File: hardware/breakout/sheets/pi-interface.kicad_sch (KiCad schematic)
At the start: 27 parts, among them J10 Barcode spare 1, J11 Barcode spare 2, J12 Barcode spare 3, J13 Eye camera trigger out (BNC), J14 Behavior camera trigger out 1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, J15 Behavior camera trigger out 2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, J16 Behavior camera trigger out 3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, J17 Behavior camera trigger out 4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, J18 Internal USB-A (sync-module p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, J7 Sync-module 40-pin GPIO heade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, J8 Barcode -> NI optocoupler (Ta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, J9 Barcode -> Intan optocoupler 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, U14 SN74LVC541APW, U15 SN74AHCT541PW, U74 SN74AHCT541PW

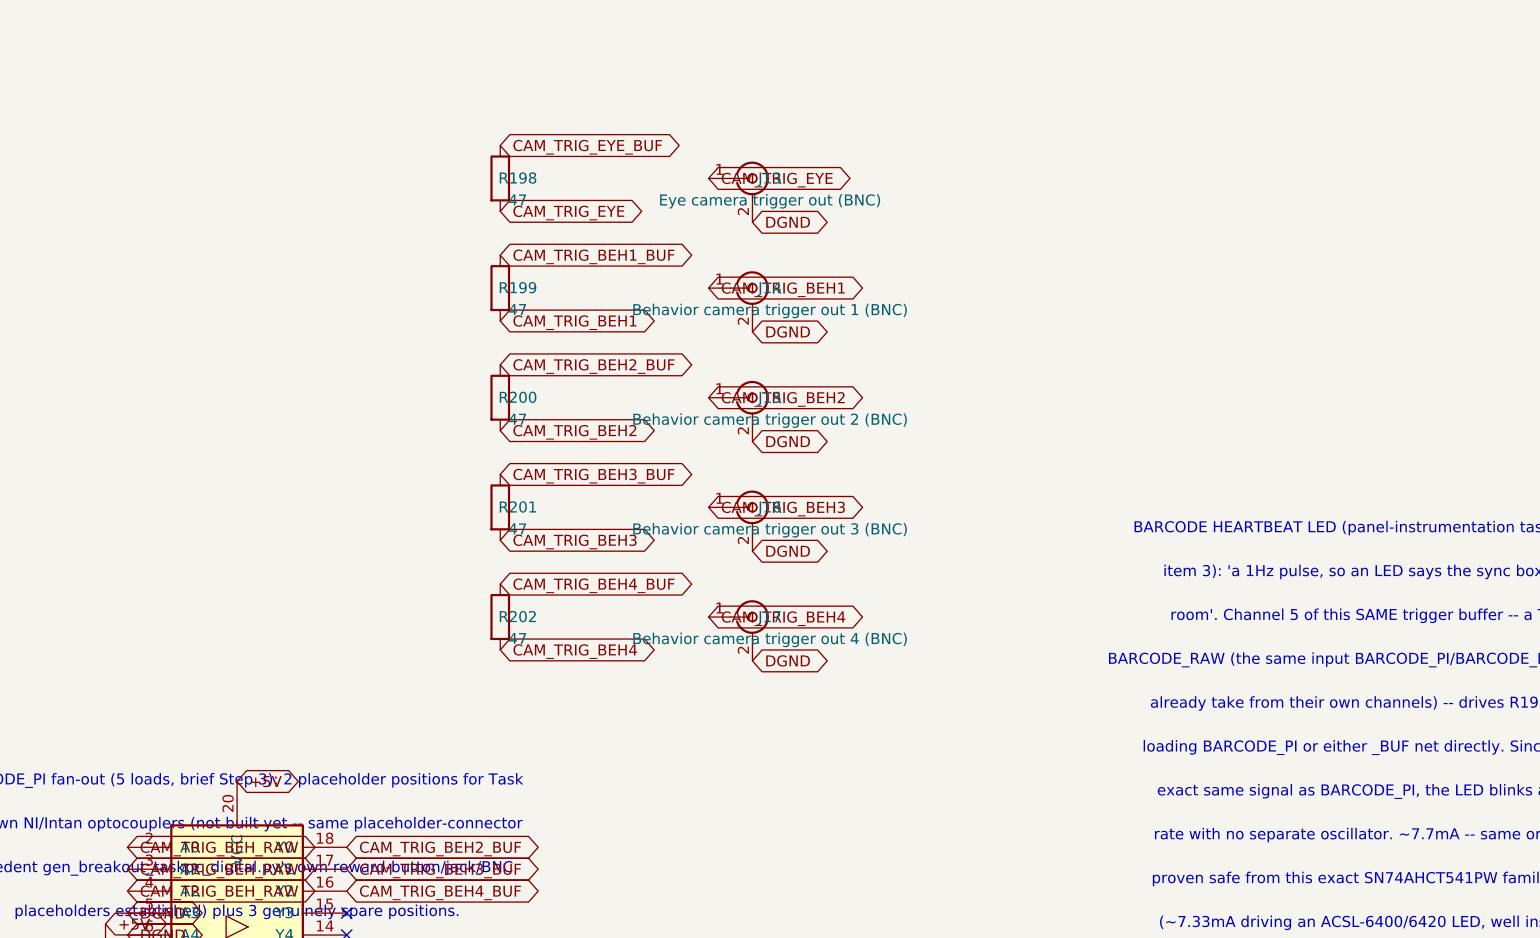
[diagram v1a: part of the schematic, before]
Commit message: fix(hardware): rebuild the connectors on their primary drawings (F6, R1, D3)
Audit step 5, the mechanical half. Three connectors changed, one of them a
fab-stopper, and none of it was visible to the netlist.

MDR68 (the fab-stopper). Rebuilt from MH drawing 3700-0121-01 rev 3.0. The
as-built footprint drilled contacts at 0.5 mm against a required 0.85 mm -- the
pins do not fit, so the board could not have been assembled -- and laid them out
as 2 rows at 2.84 mm where the drawing shows 4 staggered rows of 17 at 1.905 mm.
The 4-row stagger is what makes an 0.85 mm drill manufacturable at a 1.27 mm
mating pitch at all; the array now spans the drawing's own 41.91 mm exactly,
which is the arithmetic that confirms the reading. The claim made during the
audit that it had "no mounting holes at all" was wrong: it had two, Ø2.79 on
57.9 mm centres against the drawing's Ø2.77 on 57.93.

M12 (ruling R1). M12A_5_Panel is deleted, symbol and footprint and generator
function alike. Its contact geometry was sourced well -- IEC 61076-2-101
A-coding, cross-checked three ways -- and it made no difference, because the part
the design procures (Phoenix 1551833) terminates in AWG 22-20 wire and mounts
through the panel. It has no PCB tails, so no board-mount footprint of any
dimensions could have been right, and as built every cable insertion and every
3-4 N.m tightening loaded PCB pads directly. J1 is now a stock 5-way header where
those flying leads land; the connector stays in the order BOM as chassis
furniture.

BNC (F6). BNC_PanelMountable_Vertical puts the connector axis perpendicular to
the PCB -- a 9.65 mm barrel hole through the board -- so on a 430x240 mm board
lying flat in a 2U chassis all 31 barrels pointed at the lid rather than at the
panels. It also cost 5,654 mm2 of pad and 2,267 mm2 of removed copper on every
layer. Replaced by a right-angle dual jack built from Amphenol drawing 31-6575
rev A: 31 ports on 17 bodies, 3 spare ports, every shell still routed
individually.
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
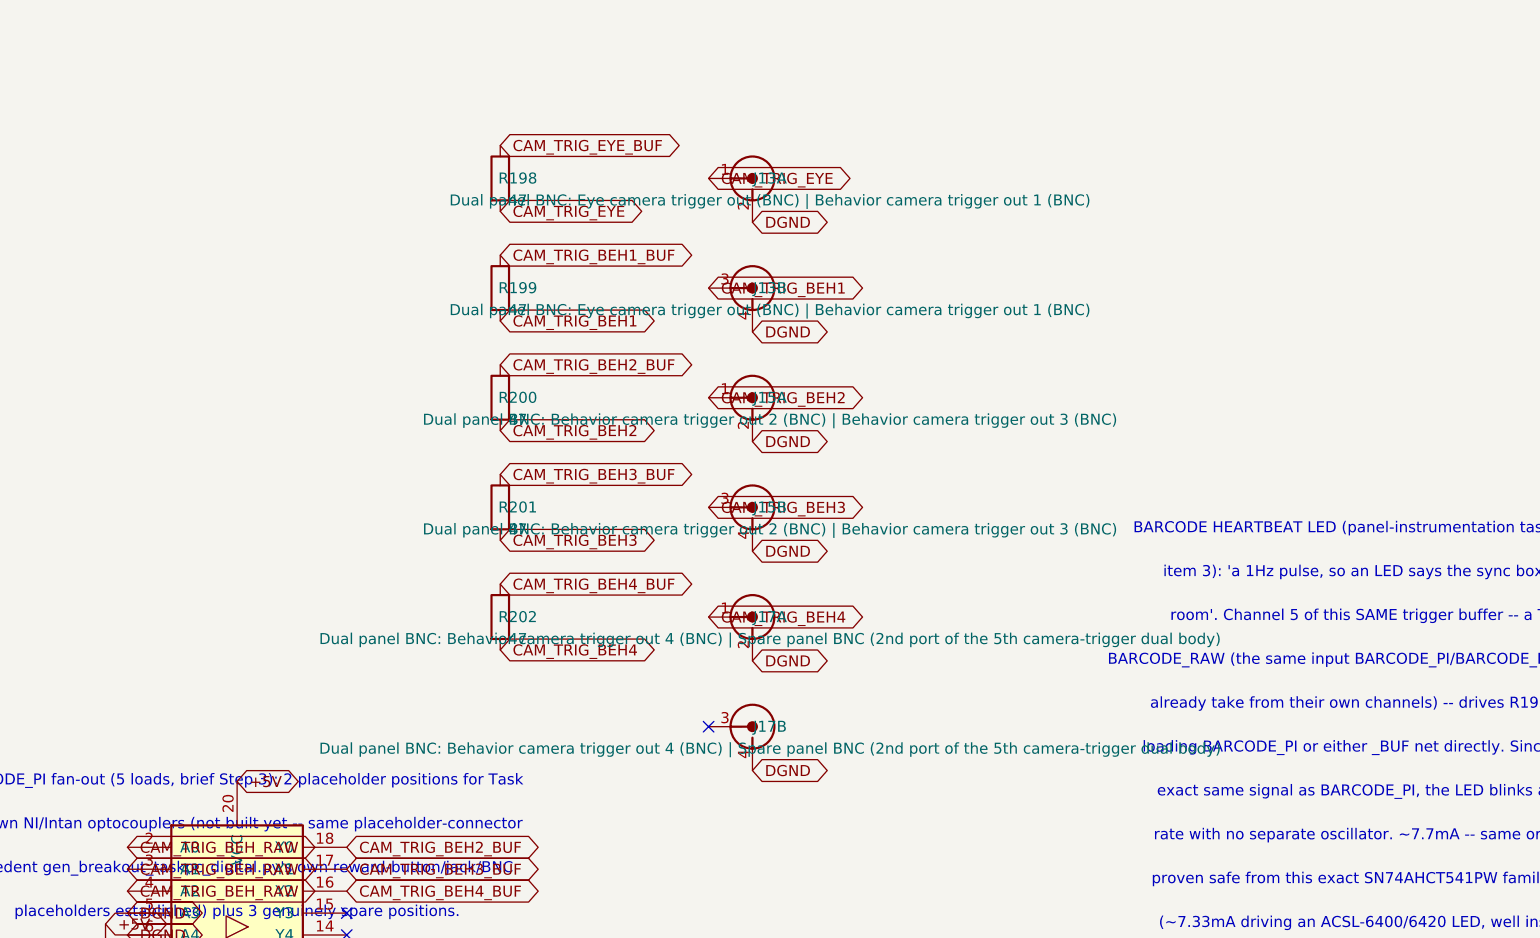
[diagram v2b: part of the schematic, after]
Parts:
- removed J13: Eye camera trigger out (BNC), Connector_Coaxial:BNC_PanelMountable_Vertical, symbol Connector:Conn_Coaxial
- removed J14: Behavior camera trigger out 1 (BNC), Connector_Coaxial:BNC_PanelMountable_Vertical, symbol Connector:Conn_Coaxial
- removed J15: Behavior camera trigger out 2 (BNC), Connector_Coaxial:BNC_PanelMountable_Vertical, symbol Connector:Conn_Coaxial
- removed J16: Behavior camera trigger out 3 (BNC), Connector_Coaxial:BNC_PanelMountable_Vertical, symbol Connector:Conn_Coaxial
- removed J17: Behavior camera trigger out 4 (BNC), Connector_Coaxial:BNC_PanelMountable_Vertical, symbol Connector:Conn_Coaxial
- added J13: Dual panel BNC: Eye camera trigger out (BNC) | Be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, wl-sync:BNC_Dual_RA_Isolated, symbol wl-sync:BNC_Dual_RA_Isolated
- added J15: Dual panel BNC: Behavior camera trigger out 2 (BN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, wl-sync:BNC_Dual_RA_Isolated, symbol wl-sync:BNC_Dual_RA_Isolated
- added J17: Dual panel BNC: Behavior camera trigger out 4 (BN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, wl-sync:BNC_Dual_RA_Isolated, symbol wl-sync:BNC_Dual_RA_Isolated
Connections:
- net CAM_TRIG_BEH1: now also J13.3 (B_In)
- net CAM_TRIG_BEH2: now also J15.1 (A_In)
- net CAM_TRIG_BEH3: now also J15.3 (B_In)
- net CAM_TRIG_BEH4: now also J17.1 (A_In)
- net CAM_TRIG_EYE: now also J13.1 (A_In)
- net DGND: now also J13.2 (A_Ext), J13.4 (B_Ext), J15.2 (A_Ext), J15.4 (B_Ext), J17.2 (A_Ext), J17.4 (B_Ext)
- no-connect marks 18 -> 19
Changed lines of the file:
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@@
 	)
 	(symbol
-		(lib_id "Connector:Conn_Coaxial")
+		(lib_id "wl-sync:BNC_Dual_RA_Isolated")
 		(at 359.41 209.55 0)
 		(unit 1)
@@
 			(effects (font (size 1.27 1.27)))
 		)
-		(property "Value" "Eye camera trigger out (BNC)"
+		(property "Value" "Dual panel BNC: Eye camera trigger out (BNC) | Behavior camera trigger out 1 (BNC)"
 			(at 361.442 212.09 0)
 			(effects (font (size 1.27 1.27)))
 		)
-		(property "Footprint" "Connector_Coaxial:BNC_PanelMountable_Vertical"
+		(property "Footprint" "wl-sync:BNC_Dual_RA_Isolated"
 			(at 359.41 209.55 0)
 			(effects (font (size 1.27 1.27)) (hide yes))
@@
 	)
 	(symbol
-		(lib_id "Connector:Conn_Coaxial")
+		(lib_id "wl-sync:BNC_Dual_RA_Isolated")
 		(at 359.41 222.25 0)
-		(unit 1)
-		(exclude_from_sim no)
-		(in_bom yes)
-		(on_board yes)
-		(dnp no)
-		(property "Reference" "J14"
+		(unit 2)
+		(exclude_from_sim no)
+		(in_bom yes)
+		(on_board yes)
+		(dnp no)
+		(property "Reference" "J13"
 			(at 361.442 222.25 0)
 			(effects (font (size 1.27 1.27)))
 		)
-		(property "Value" "Behavior camera trigger out 1 (BNC)"
+		(property "Value" "Dual panel BNC: Eye camera trigger out (BNC) | Behavior camera trigger out 1 (BNC)"
 			(at 361.442 224.79 0)
 			(effects (font (size 1.27 1.27)))
 		)
-		(property "Footprint" "Connector_Coaxial:BNC_PanelMountable_Vertical"
+		(property "Footprint" "wl-sync:BNC_Dual_RA_Isolated"
 			(at 359.41 222.25 0)
 			(effects (font (size 1.27 1.27)) (hide yes))
@@
 			(effects (font (size 1.27 1.27)) (hide yes))
 		)
-		(pin "1")
-		(pin "2")
-		(instances
-			(project "breakout"
-				(path "/d2c4d978-5db4-46d9-a1cd-a7af0aeb1700/9354f636-4238-4ab3-b39b-61056b5cf16b"
-					(reference "J14") (unit 1)
+		(pin "3")
+		(pin "4")
+		(instances
+			(project "breakout"
+				(path "/d2c4d978-5db4-46d9-a1cd-a7af0aeb1700/9354f636-4238-4ab3-b39b-61056b5cf16b"
+					(reference "J13") (unit 2)
 				)
 			)
@@
 	)
 	(symbol
-		(lib_id "Connector:Conn_Coaxial")
+		(lib_id "wl-sync:BNC_Dual_RA_Isolated")
 		(at 359.41 234.95000000000002 0)
 		(unit 1)
@@
 			(effects (font (size 1.27 1.27)))
 		)
-		(property "Value" "Behavior camera trigger out 2 (BNC)"
+		(property "Value" "Dual panel BNC: Behavior camera trigger out 2 (BNC) | Behavior camera trigger out 3 (BNC)"
 			(at 361.442 237.49 0)
 			(effects (font (size 1.27 1.27)))
 		)
-		(property "Footprint" "Connector_Coaxial:BNC_PanelMountable_Vertical"
+		(property "Footprint" "wl-sync:BNC_Dual_RA_Isolated"
 			(at 359.41 234.95000000000002 0)
 			(effects (font (size 1.27 1.27)) (hide yes))
@@
 	)
 	(symbol
-		(lib_id "Connector:Conn_Coaxial")
+		(lib_id "wl-sync:BNC_Dual_RA_Isolated")
 		(at 359.41 247.65 0)
-		(unit 1)
-		(exclude_from_sim no)
-		(in_bom yes)
-		(on_board yes)
-		(dnp no)
-		(property "Reference" "J16"
+		(unit 2)
+		(exclude_from_sim no)
+		(in_bom yes)
+		(on_board yes)
+		(dnp no)
+		(property "Reference" "J15"
 			(at 361.442 247.65 0)
 			(effects (font (size 1.27 1.27)))
 		)
-		(property "Value" "Behavior camera trigger out 3 (BNC)"
+		(property "Value" "Dual panel BNC: Behavior camera trigger out 2 (BNC) | Behavior camera trigger out 3 (BNC)"
 			(at 361.442 250.19 0)
 			(effects (font (size 1.27 1.27)))
 		)
-		(property "Footprint" "Connector_Coaxial:BNC_PanelMountable_Vertical"
+		(property "Footprint" "wl-sync:BNC_Dual_RA_Isolated"
 			(at 359.41 247.65 0)
 			(effects (font (size 1.27 1.27)) (hide yes))
@@
 			(effects (font (size 1.27 1.27)) (hide yes))
 		)
-		(pin "1")
-		(pin "2")
-		(instances
-			(project "breakout"
-				(path "/d2c4d978-5db4-46d9-a1cd-a7af0aeb1700/9354f636-4238-4ab3-b39b-61056b5cf16b"
-					(reference "J16") (unit 1)
+		(pin "3")
+		(pin "4")
+		(instances
+			(project "breakout"
+				(path "/d2c4d978-5db4-46d9-a1cd-a7af0aeb1700/9354f636-4238-4ab3-b39b-61056b5cf16b"
+					(reference "J15") (unit 2)
 				)
 			)
@@
 	)
 	(symbol
-		(lib_id "Connector:Conn_Coaxial")
+		(lib_id "wl-sync:BNC_Dual_RA_Isolated")
 		(at 359.41 260.35 0)
 		(unit 1)
@@
 			(effects (font (size 1.27 1.27)))
 		)
-		(property "Value" "Behavior camera trigger out 4 (BNC)"
+		(property "Value" "Dual panel BNC: Behavior camera trigger out 4 (BNC) | Spare panel BNC (2nd port of the 5th camera-trigger dual body)"
 			(at 361.442 262.89000000000004 0)
 			(effects (font (size 1.27 1.27)))
 		)
-		(property "Footprint" "Connector_Coaxial:BNC_PanelMountable_Vertical"
+		(property "Footprint" "wl-sync:BNC_Dual_RA_Isolated"
 			(at 359.41 260.35 0)
 			(effects (font (size 1.27 1.27)) (hide yes))
@@
 			(effects (font (size 1.27 1.27)) (hide yes))
 		)
+	)
+	(symbol
+		(lib_id "wl-sync:BNC_Dual_RA_Isolated")
+		(at 359.41 273.05 0)
+		(unit 2)
+		(exclude_from_sim no)
+		(in_bom yes)
+		(on_board yes)
+		(dnp no)
+		(property "Reference" "J17"
+			(at 361.442 273.05 0)
+			(effects (font (size 1.27 1.27)))
+		)
+		(property "Value" "Dual panel BNC: Behavior camera trigger out 4 (BNC) | Spare panel BNC (2nd port of the 5th camera-trigger dual body)"
+			(at 361.442 275.59000000000003 0)
+			(effects (font (size 1.27 1.27)))
+		)
+		(property "Footprint" "wl-sync:BNC_Dual_RA_Isolated"
+			(at 359.41 273.05 0)
+			(effects (font (size 1.27 1.27)) (hide yes))
+		)
+		(property "Datasheet" ""
+			(at 359.41 273.05 0)
+			(effects (font (size 1.27 1.27)) (hide yes))
+		)
+		(pin "3")
+		(pin "4")
+		(instances
+			(project "breakout"
+				(path "/d2c4d978-5db4-46d9-a1cd-a7af0aeb1700/9354f636-4238-4ab3-b39b-61056b5cf16b"
+					(reference "J17") (unit 2)
+				)
+			)
+		)
+	)
+	(no_connect
+		(at 354.33000000000004 273.05)
+	)
+	(global_label "DGND"
+		(shape bidirectional)
+		(at 359.41 278.13 0)
+		(effects (font (size 1.27 1.27)) (justify left))
+		(property "Intersheetrefs" "${INTERSHEET_REFS}"
+			(at 359.41 278.13 0)
+			(effects (font (size 1.27 1.27)) (hide yes))
+		)
